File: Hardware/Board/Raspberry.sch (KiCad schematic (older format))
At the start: 5 parts, among them J6 Raspberry_Pi_2_3, U13 ESP-12F

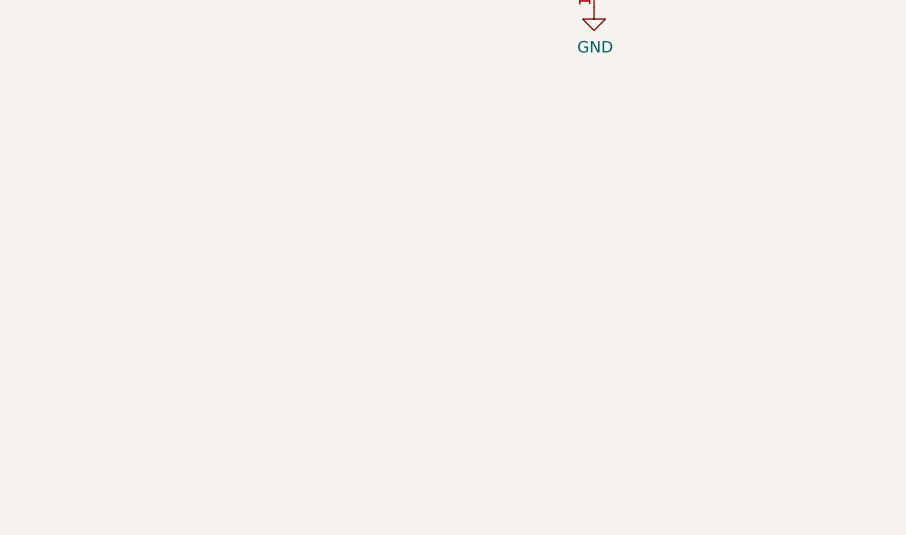
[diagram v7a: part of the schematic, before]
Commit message: GSM Modul SIM800L eingefügt, Spannung MCU Board umgenannt
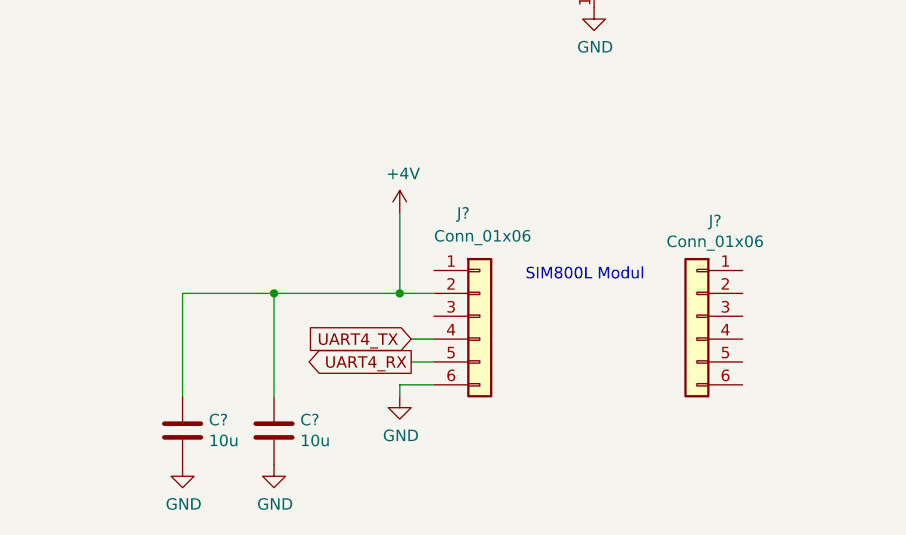
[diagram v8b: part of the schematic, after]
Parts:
- added C? (x2): 10u, Capacitor_SMD:C_1210_3225Metric, symbol Device:C
- added J? (x2): Conn_01x06, symbol Connector_Generic:Conn_01x06
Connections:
- net GND: now also C?.2, C?.2, J?.6 (Pin_6)
- net UART4_RX: now also J?.5 (Pin_5)
- net UART4_TX: now also J?.4 (Pin_4)
- new net +4V: C?.1, C?.1, J?.2 (Pin_2)
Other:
- note added: "SIM800L Modul\n"
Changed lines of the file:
@@
 	7950 1250 7950 1350
 Connection ~ 7950 1350
+$Comp
+L Connector_Generic:Conn_01x06 J?
+U 1 1 60626CBA
+P 7450 4800
+F 0 "J?" H 7350 5250 50  0000 L CNN
+F 1 "Conn_01x06" H 7250 5150 50  0000 L CNN
+F 2 "" H 7450 4800 50  0001 C CNN
+F 3 "~" H 7450 4800 50  0001 C CNN
+	1    7450 4800
+	1    0    0    -1
+$EndComp
+$Comp
+L Connector_Generic:Conn_01x06 J?
+U 1 1 60626D7E
+P 8400 4800
+F 0 "J?" H 8320 5217 50  0000 C CNN
+F 1 "Conn_01x06" H 8320 5126 50  0000 C CNN
+F 2 "" H 8400 4800 50  0001 C CNN
+F 3 "~" H 8400 4800 50  0001 C CNN
+	1    8400 4800
+	-1   0    0    -1
+$EndComp
+$Comp
+L power:GND #PWR?
+U 1 1 606274EA
+P 7100 5150
+F 0 "#PWR?" H 7100 4900 50  0001 C CNN
+F 1 "GND" H 7105 4977 50  0000 C CNN
+F 2 "" H 7100 5150 50  0001 C CNN
+F 3 "" H 7100 5150 50  0001 C CNN
+	1    7100 5150
+	1    0    0    -1
+$EndComp
+$Comp
+L stmbl:+4V #PWR?
+U 1 1 60627B42
+P 7100 4350
+F 0 "#PWR?" H 7100 4200 50  0001 C CNN
+F 1 "+4V" H 7115 4523 50  0000 C CNN
+F 2 "" H 7100 4350 50  0001 C CNN
+F 3 "" H 7100 4350 50  0001 C CNN
+	1    7100 4350
+	1    0    0    -1
+$EndComp
+$Comp
+L Device:C C?
+U 1 1 60627C50
+P 6550 5300
+F 0 "C?" H 6665 5346 50  0000 L CNN
+F 1 "10u" H 6665 5255 50  0000 L CNN
+F 2 "Capacitor_SMD:C_1210_3225Metric" H 6588 5150 50  0001 C CNN
+F 3 "~" H 6550 5300 50  0001 C CNN
+	1    6550 5300
+	1    0    0    -1
+$EndComp
+$Comp
+L power:GND #PWR?
+U 1 1 60627C57
+P 6550 5450
+F 0 "#PWR?" H 6550 5200 50  0001 C CNN
+F 1 "GND" H 6555 5277 50  0000 C CNN
+F 2 "" H 6550 5450 50  0001 C CNN
+F 3 "" H 6550 5450 50  0001 C CNN
+	1    6550 5450
+	1    0    0    -1
+$EndComp
+$Comp
+L Device:C C?
+U 1 1 60628290
+P 6150 5300
+F 0 "C?" H 6265 5346 50  0000 L CNN
+F 1 "10u" H 6265 5255 50  0000 L CNN
+F 2 "Capacitor_SMD:C_1210_3225Metric" H 6188 5150 50  0001 C CNN
+F 3 "~" H 6150 5300 50  0001 C CNN
+	1    6150 5300
+	1    0    0    -1
+$EndComp
+$Comp
+L power:GND #PWR?
+U 1 1 60628297
+P 6150 5450
+F 0 "#PWR?" H 6150 5200 50  0001 C CNN
+F 1 "GND" H 6155 5277 50  0000 C CNN
+F 2 "" H 6150 5450 50  0001 C CNN
+F 3 "" H 6150 5450 50  0001 C CNN
+	1    6150 5450
+	1    0    0    -1
+$EndComp
+Wire Wire Line
+	7250 5100 7100 5100
+Wire Wire Line
+	7100 5100 7100 5150
+Wire Wire Line
+	7250 4700 7100 4700
+Wire Wire Line
+	7100 4700 7100 4350
+Wire Wire Line
+	7100 4700 6550 4700
+Wire Wire Line
+	6150 4700 6150 5150
+Connection ~ 7100 4700
+Wire Wire Line
+	6550 5150 6550 4700
+Connection ~ 6550 4700
+Wire Wire Line
+	6550 4700 6150 4700
+Text GLabel 7150 4900 0    50   Input ~ 0
+UART4_TX
+Text GLabel 7150 5000 0    50   Output ~ 0
+UART4_RX
+Wire Wire Line
+	7250 4900 7150 4900
+Wire Wire Line
+	7250 5000 7150 5000
+Text Notes 7650 4650 0    50   ~ 0
+SIM800L Modul\n
 $EndSCHEMATC
